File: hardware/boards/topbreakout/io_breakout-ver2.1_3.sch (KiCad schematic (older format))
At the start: 7 parts, among them J1 WURTH_ELECTRONICS_61400413321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, J2 MOLEX_52892-3033MOLEX_52892-3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, J3 USB-A-S-X-X-VT

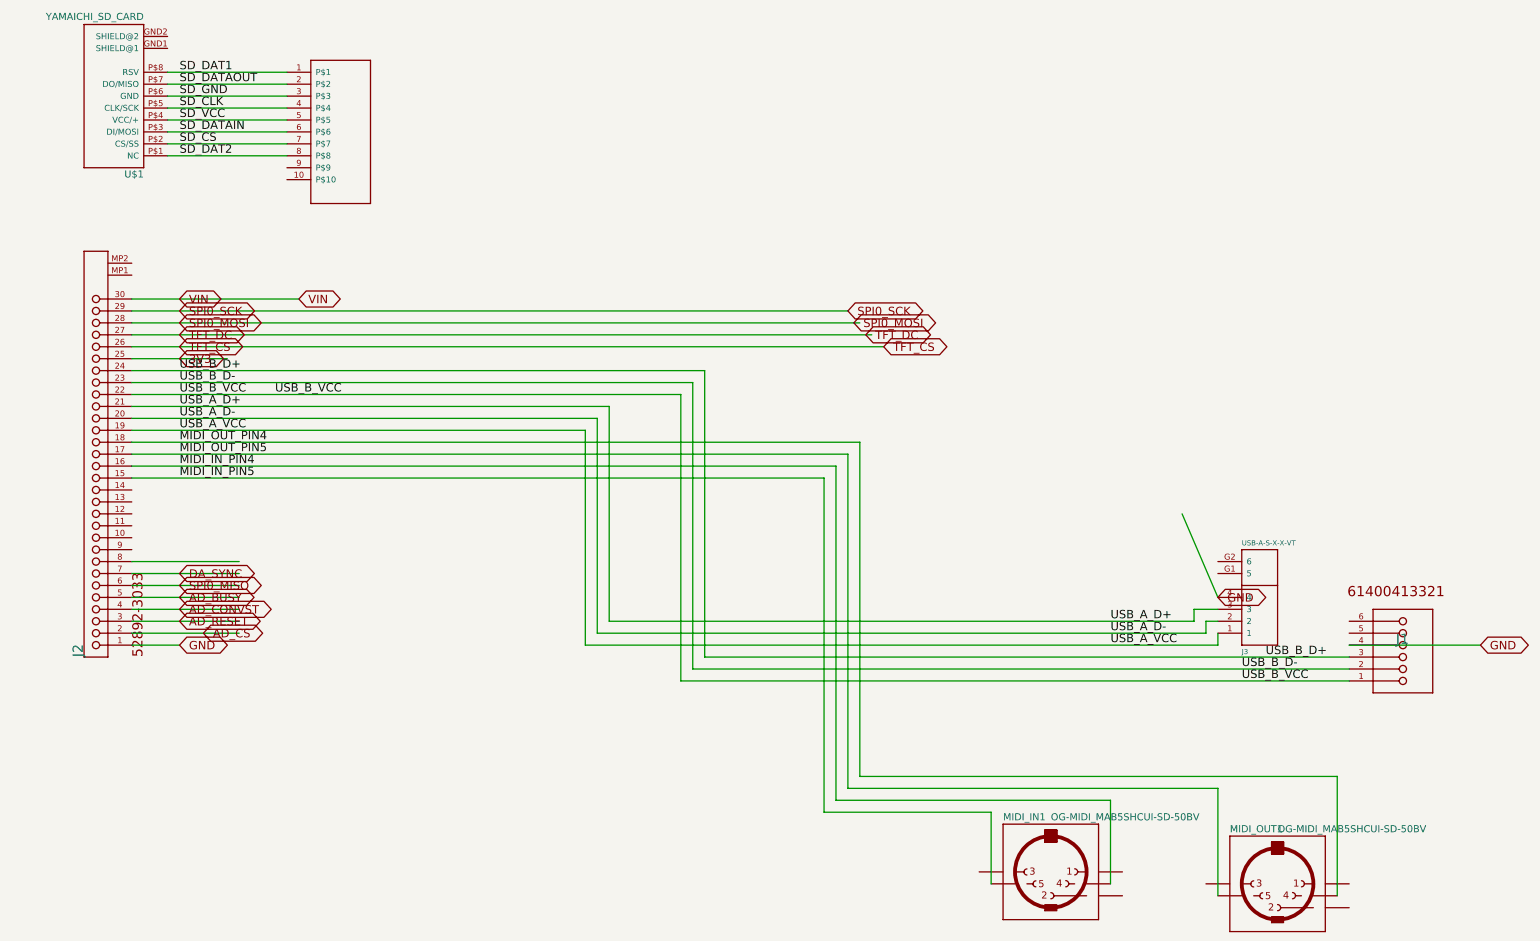
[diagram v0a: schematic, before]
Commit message: TopBreakout improvements
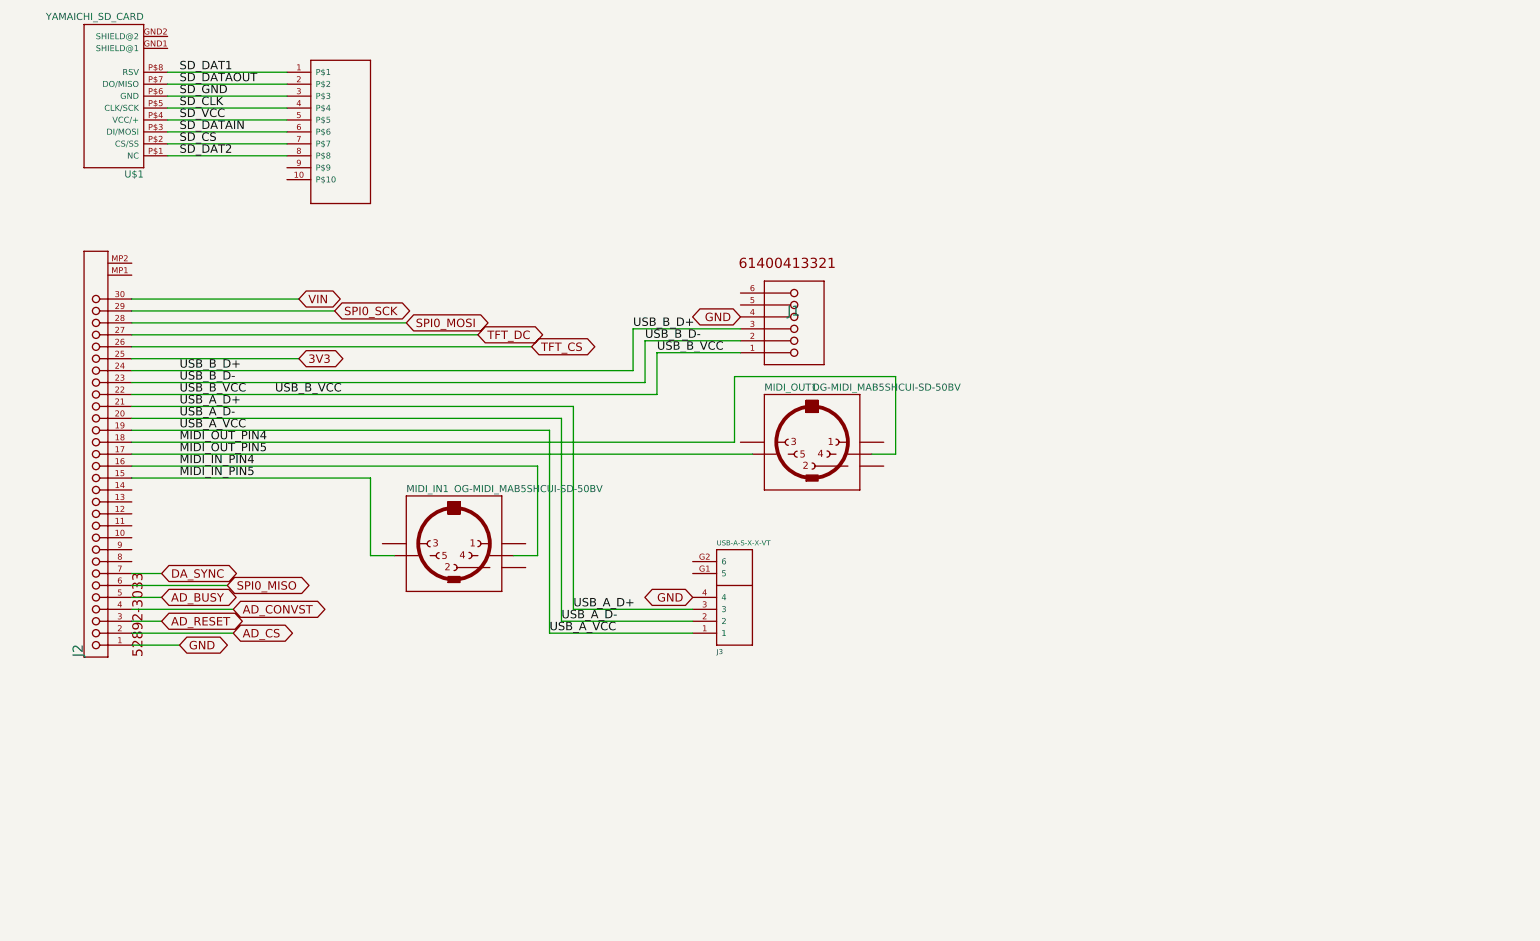
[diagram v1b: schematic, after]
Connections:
- wire segments 63 -> 51
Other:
- moved on the sheet: J1, J3, MIDI_IN1, MIDI_OUT1
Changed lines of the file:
@@
 EESchema Schematic File Version 4
+LIBS:TopBreakout-cache
 EELAYER 30 0
 EELAYER END
@@
 $EndDescr
 Wire Wire Line
-	11600 6300 6000 6300
-Wire Wire Line
-	6000 6300 6000 3900
-Wire Wire Line
-	6000 3900 1400 3900
-Text Label 10700 6300 0    70   ~ 0
+	6500 3550 5800 3550
+Wire Wire Line
+	5800 3550 5800 3900
+Wire Wire Line
+	5800 3900 1400 3900
+Text Label 5800 3550 0    70   ~ 0
 USB_B_VCC
 Text Label 2600 3900 0    70   ~ 0
@@
 USB_B_VCC
 Wire Wire Line
-	11600 6200 6100 6200
-Wire Wire Line
-	6100 6200 6100 3800
-Wire Wire Line
-	6100 3800 1400 3800
-Text Label 10700 6200 0    70   ~ 0
+	6500 3450 5700 3450
+Wire Wire Line
+	5700 3450 5700 3800
+Wire Wire Line
+	5700 3800 1400 3800
+Text Label 5700 3450 0    70   ~ 0
 USB_B_D-
 Text Label 1800 3800 0    70   ~ 0
 USB_B_D-
 Wire Wire Line
-	11600 6100 6200 6100
-Wire Wire Line
-	6200 6100 6200 3700
-Wire Wire Line
-	6200 3700 1400 3700
-Text Label 10900 6100 0    70   ~ 0
+	6500 3350 5600 3350
+Wire Wire Line
+	5600 3350 5600 3700
+Wire Wire Line
+	5600 3700 1400 3700
+Text Label 5600 3350 0    70   ~ 0
 USB_B_D+
 Text Label 1800 3700 0    70   ~ 0
 USB_B_D+
-Wire Wire Line
-	10500 5600 10200 4900
-Text GLabel 10500 5600 2    70   BiDi ~ 0
+Text GLabel 6100 5600 0    70   BiDi ~ 0
 GND
-Wire Wire Line
-	11600 6000 12700 6000
-Text GLabel 12700 6000 2    70   BiDi ~ 0
+Text GLabel 6500 3250 0    70   BiDi ~ 0
 GND
 Wire Wire Line
@@
 GND
 Wire Wire Line
-	10500 5900 10500 6000
-Wire Wire Line
-	10500 6000 5200 6000
-Wire Wire Line
-	5200 6000 5200 4200
-Wire Wire Line
-	5200 4200 1400 4200
-Text Label 9600 6000 0    70   ~ 0
+	4900 5900 4900 4200
+Wire Wire Line
+	4900 4200 1400 4200
+Text Label 4900 5900 0    70   ~ 0
 USB_A_VCC
 Text Label 1800 4200 0    70   ~ 0
 USB_A_VCC
 Wire Wire Line
-	10500 5700 10300 5700
-Wire Wire Line
-	10300 5700 10300 5800
-Wire Wire Line
-	10300 5800 5400 5800
-Wire Wire Line
-	5400 5800 5400 4000
-Wire Wire Line
-	5400 4000 1400 4000
-Text Label 9600 5800 0    70   ~ 0
+	5100 5700 5100 4000
+Wire Wire Line
+	5100 4000 1400 4000
+Text Label 5100 5700 0    70   ~ 0
 USB_A_D+
 Text Label 1800 4000 0    70   ~ 0
 USB_A_D+
 Wire Wire Line
-	1400 3500 7700 3500
-Text GLabel 7700 3500 2    70   BiDi ~ 0
+	1400 3500 4750 3500
+Text GLabel 4750 3500 2    70   BiDi ~ 0
 TFT_CS
-Text GLabel 1800 3500 2    70   BiDi ~ 0
-TFT_CS
-Wire Wire Line
-	1400 3400 7600 3400
-Text GLabel 7550 3400 2    70   BiDi ~ 0
+Wire Wire Line
+	1400 3400 4300 3400
+Text GLabel 4300 3400 2    70   BiDi ~ 0
 TFT_DC
-Text GLabel 1800 3400 2    70   BiDi ~ 0
-TFT_DC
-Wire Wire Line
-	1400 3200 7400 3200
-Text GLabel 7400 3200 2    70   BiDi ~ 0
+Wire Wire Line
+	1400 3200 3100 3200
+Text GLabel 3100 3200 2    70   BiDi ~ 0
 SPI0_SCK
-Text GLabel 1800 3200 2    70   BiDi ~ 0
-SPI0_SCK
-Wire Wire Line
-	1400 3300 7500 3300
-Text GLabel 7450 3300 2    70   BiDi ~ 0
-SPI0_MOSI
-Text GLabel 1800 3300 2    70   BiDi ~ 0
+Wire Wire Line
+	1400 3300 3700 3300
+Text GLabel 3700 3300 2    70   BiDi ~ 0
 SPI0_MOSI
 Wire Wire Line
@@
 Text GLabel 2800 3100 2    70   BiDi ~ 0
 VIN
-Text GLabel 1800 3100 2    70   BiDi ~ 0
-VIN
-Wire Wire Line
-	1400 4600 7200 4600
-Wire Wire Line
-	7200 4600 7200 7400
-Wire Wire Line
-	8600 8000 8600 7400
-Wire Wire Line
-	7200 7400 8600 7400
+Wire Wire Line
+	1400 4600 3400 4600
 Text Label 1800 4600 0    70   ~ 0
 MIDI_IN_PIN5
-Wire Wire Line
-	1400 4500 7300 4500
-Wire Wire Line
-	7300 4500 7300 7300
-Wire Wire Line
-	9600 8000 9600 7300
-Wire Wire Line
-	7300 7300 9600 7300
 Text Label 1800 4500 0    70   ~ 0
 MIDI_IN_PIN4
-Wire Wire Line
-	1400 4400 7400 4400
-Wire Wire Line
-	7400 4400 7400 7200
-Wire Wire Line
-	10500 8100 10500 7200
-Wire Wire Line
-	7400 7200 10500 7200
 Text Label 1800 4400 0    70   ~ 0
 MIDI_OUT_PIN5
 Wire Wire Line
-	1400 4300 7500 4300
-Wire Wire Line
-	7500 4300 7500 7100
-Wire Wire Line
-	11500 8100 11500 7100
-Wire Wire Line
-	7500 7100 11500 7100
+	1400 4300 6450 4300
+Wire Wire Line
+	6450 4300 6450 3750
+Wire Wire Line
+	6450 3750 7800 3750
 Text Label 1800 4300 0    70   ~ 0
 MIDI_OUT_PIN4
 Wire Wire Line
-	1400 4100 5300 4100
-Wire Wire Line
-	5300 4100 5300 5900
-Wire Wire Line
-	10500 5800 10400 5800
-Wire Wire Line
-	10400 5800 10400 5900
-Wire Wire Line
-	5300 5900 10400 5900
-Text Label 9600 5900 0    70   ~ 0
+	1400 4100 5000 4100
+Wire Wire Line
+	5000 4100 5000 5800
+Text Label 5000 5800 0    70   ~ 0
 USB_A_D-
 Text Label 1800 4100 0    70   ~ 0
@@
 SD_DAT2
 Wire Wire Line
-	1400 5900 2300 5900
-Text GLabel 2000 5900 2    70   BiDi ~ 0
+	1400 5900 2250 5900
+Text GLabel 2250 5900 2    70   BiDi ~ 0
 AD_CS
 Wire Wire Line
-	1400 5800 2300 5800
-Text GLabel 1800 5800 2    70   BiDi ~ 0
+	1400 5800 1650 5800
+Text GLabel 1650 5800 2    70   BiDi ~ 0
 AD_RESET
 Wire Wire Line
-	1400 5700 2300 5700
-Text GLabel 1800 5700 2    70   BiDi ~ 0
+	1400 5700 2250 5700
+Text GLabel 2250 5700 2    70   BiDi ~ 0
 AD_CONVST
 Wire Wire Line
-	1400 5600 2300 5600
-Text GLabel 1800 5600 2    70   BiDi ~ 0
+	1400 5600 1650 5600
+Text GLabel 1650 5600 2    70   BiDi ~ 0
 AD_BUSY
 Wire Wire Line
-	1400 5500 2300 5500
-Text GLabel 1800 5500 2    70   BiDi ~ 0
+	1400 5500 2200 5500
+Text GLabel 2200 5500 2    70   BiDi ~ 0
 SPI0_MISO
 Wire Wire Line
-	1400 5400 2300 5400
-Text GLabel 1800 5400 2    70   BiDi ~ 0
+	1400 5400 1650 5400
+Text GLabel 1650 5400 2    70   BiDi ~ 0
 DA_SYNC
 Wire Wire Line
-	1400 5300 2300 5300
-Wire Wire Line
-	1400 3600 2200 3600
-Text GLabel 1800 3600 2    70   BiDi ~ 0
+	1400 3600 2800 3600
+Text GLabel 2800 3600 2    70   BiDi ~ 0
 3V3
 $Comp
 L TopBreakout-eagle-import:WURTH_ELECTRONICS_61400413321WURTH_ELECTRONICS_61400413321_0_0 J1
 U 1 1 92202B0B
-P 12200 6100
+P 7100 3350
 AR Path="/92202B0B" Ref="J1"  Part="1"
 AR Path="/5D7F42FA/92202B0B" Ref="J1"  Part="1"
-F 0 "J1" H 12300 6000 85  0000 L TNN
-F 1 "WURTH_ELECTRONICS_61400413321WURTH_ELECTRONICS_61400413321_0_0" H 12200 6100 50  0001 C CNN
-F 2 "topbreakout:WURTH_ELECTRONICS_61400413321_0" H 12200 6100 50  0001 C CNN
-F 3 "" H 12200 6100 50  0001 C CNN
-	1    12200 6100
+F 0 "J1" H 7200 3250 85  0000 L TNN
+F 1 "WURTH_ELECTRONICS_61400413321WURTH_ELECTRONICS_61400413321_0_0" H 7100 3350 50  0001 C CNN
+F 2 "topbreakout:WURTH_ELECTRONICS_61400413321_0" H 7100 3350 50  0001 C CNN
+F 3 "" H 7100 3350 50  0001 C CNN
+	1    7100 3350
 	-1   0    0    1
 $EndComp
@@
 L TopBreakout-eagle-import:USB-A-S-X-X-VT J3
 U 1 1 83A3164B
-P 10500 5900
+P 6100 5900
 AR Path="/83A3164B" Ref="J3"  Part="1"
 AR Path="/5D7F42FA/83A3164B" Ref="J3"  Part="1"
-F 0 "J3" H 10700 6031 42  0000 L BNN
-F 1 "USB-A-S-X-X-VT" H 10700 5120 42  0000 L BNN
-F 2 "topbreakout:USB-A-S-X-X-VT" H 10500 5900 50  0001 C CNN
-F 3 "" H 10500 5900 50  0001 C CNN
-	1    10500 5900
+F 0 "J3" H 6300 6031 42  0000 L BNN
+F 1 "USB-A-S-X-X-VT" H 6300 5120 42  0000 L BNN
+F 2 "topbreakout:USB-A-S-X-X-VT" H 6100 5900 50  0001 C CNN
+F 3 "" H 6100 5900 50  0001 C CNN
+	1    6100 5900
 	1    0    0    1
-$EndComp
-$Comp
-L TopBreakout-eagle-import:OG-MIDI_MAB5SHCUI-SD-50BV MIDI_IN
-U 1 1 1C421DBC
-P 9100 7900
-AR Path="/1C421DBC" Ref="MIDI_IN"  Part="1"
-AR Path="/5D7F42FA/1C421DBC" Ref="MIDI_IN1"  Part="1"
-F 0 "MIDI_IN1" H 8700 8325 59  0000 L BNN
-F 1 "OG-MIDI_MAB5SHCUI-SD-50BV" H 9100 8325 59  0000 L BNN
-F 2 "topbreakout:OG-MIDI_SD-50BV" H 9100 7900 50  0001 C CNN
-F 3 "" H 9100 7900 50  0001 C CNN
-	1    9100 7900
-	1    0    0    -1
 $EndComp
 $Comp
 L TopBreakout-eagle-import:OG-MIDI_MAB5SHCUI-SD-50BV MIDI_OUT
 U 1 1 74EA5AF5
-P 11000 8000
+P 7100 4300
 AR Path="/74EA5AF5" Ref="MIDI_OUT"  Part="1"
 AR Path="/5D7F42FA/74EA5AF5" Ref="MIDI_OUT1"  Part="1"
-F 0 "MIDI_OUT1" H 10600 8425 59  0000 L BNN
-F 1 "OG-MIDI_MAB5SHCUI-SD-50BV" H 11000 8425 59  0000 L BNN
-F 2 "topbreakout:OG-MIDI_SD-50BV" H 11000 8000 50  0001 C CNN
-F 3 "" H 11000 8000 50  0001 C CNN
-	1    11000 8000
+F 0 "MIDI_OUT1" H 6700 4725 59  0000 L BNN
+F 1 "OG-MIDI_MAB5SHCUI-SD-50BV" H 7100 4725 59  0000 L BNN
+F 2 "topbreakout:OG-MIDI_SD-50BV" H 7100 4300 50  0001 C CNN
+F 3 "" H 7100 4300 50  0001 C CNN
+	1    7100 4300
 	1    0    0    -1
 $EndComp
@@
 	-1   0    0    -1
 $EndComp
+Wire Wire Line
+	3400 4600 3400 5250
+Wire Wire Line
+	6100 5900 4900 5900
+$Comp
+L TopBreakout-eagle-import:OG-MIDI_MAB5SHCUI-SD-50BV MIDI_IN
+U 1 1 1C421DBC
+P 4100 5150
+AR Path="/1C421DBC" Ref="MIDI_IN"  Part="1"
+AR Path="/5D7F42FA/1C421DBC" Ref="MIDI_IN1"  Part="1"
+F 0 "MIDI_IN1" H 3700 5575 59  0000 L BNN
+F 1 "OG-MIDI_MAB5SHCUI-SD-50BV" H 4100 5575 59  0000 L BNN
+F 2 "topbreakout:OG-MIDI_SD-50BV" H 4100 5150 50  0001 C CNN
+F 3 "" H 4100 5150 50  0001 C CNN
+	1    4100 5150
+	1    0    0    -1
+$EndComp
+Wire Wire Line
+	3400 5250 3600 5250
+Wire Wire Line
+	1400 4500 4800 4500
+Wire Wire Line
+	4600 5250 4800 5250
+Wire Wire Line
+	4800 5250 4800 4500
+Wire Wire Line
+	7600 4400 7800 4400
+Wire Wire Line
+	7800 4400 7800 3750
+Wire Wire Line
+	1400 4400 6600 4400
+Wire Wire Line
+	5100 5700 6100 5700
+Wire Wire Line
+	5000 5800 6100 5800
 $EndSCHEMATC

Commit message: cleanup
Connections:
- net AVSS: now reaches J2.10
- net AVSS: now also J2.9
- net AVDD: now reaches J2.12
- net AVDD: now also J2.13
- no-connect marks 0 -> 3
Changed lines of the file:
@@
 Wire Wire Line
 	5000 5800 6100 5800
+Wire Wire Line
+	1400 5200 1400 5100
+Wire Wire Line
+	1400 4900 1400 4800
+Wire Wire Line
+	1400 4800 1800 4800
+Connection ~ 1400 4800
+Wire Wire Line
+	1400 5100 1800 5100
+Connection ~ 1400 5100
+NoConn ~ 1400 5300
+NoConn ~ 1400 5000
+NoConn ~ 1400 4700
+Text GLabel 1800 4800 2    61   Input ~ 0
+AVDD
+Text GLabel 1800 5100 2    61   Input ~ 0
+AVSS
 $EndSCHEMATC

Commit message: minor
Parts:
- added J5: Conn_01x40, Connectors_TE-Connectivity:TE_2-84953-7_1x27_P1.0mm_Horizontal, symbol Connector_Generic:Conn_01x40
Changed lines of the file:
@@
 Text GLabel 1800 5100 2    61   Input ~ 0
 AVSS
+$Comp
+L Connector_Generic:Conn_01x40 J5
+U 1 1 5D8E7BFB
+P 550 4100
+F 0 "J5" H 468 1875 50  0000 C CNN
+F 1 "Conn_01x40" H 468 1966 50  0000 C CNN
+F 2 "Connectors_TE-Connectivity:TE_2-84953-7_1x27_P1.0mm_Horizontal" H 550 4100 50  0001 C CNN
+F 3 "~" H 550 4100 50  0001 C CNN
+	1    550  4100
+	-1   0    0    1
+$EndComp
 $EndSCHEMATC
